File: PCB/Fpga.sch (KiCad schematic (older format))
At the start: 58 parts

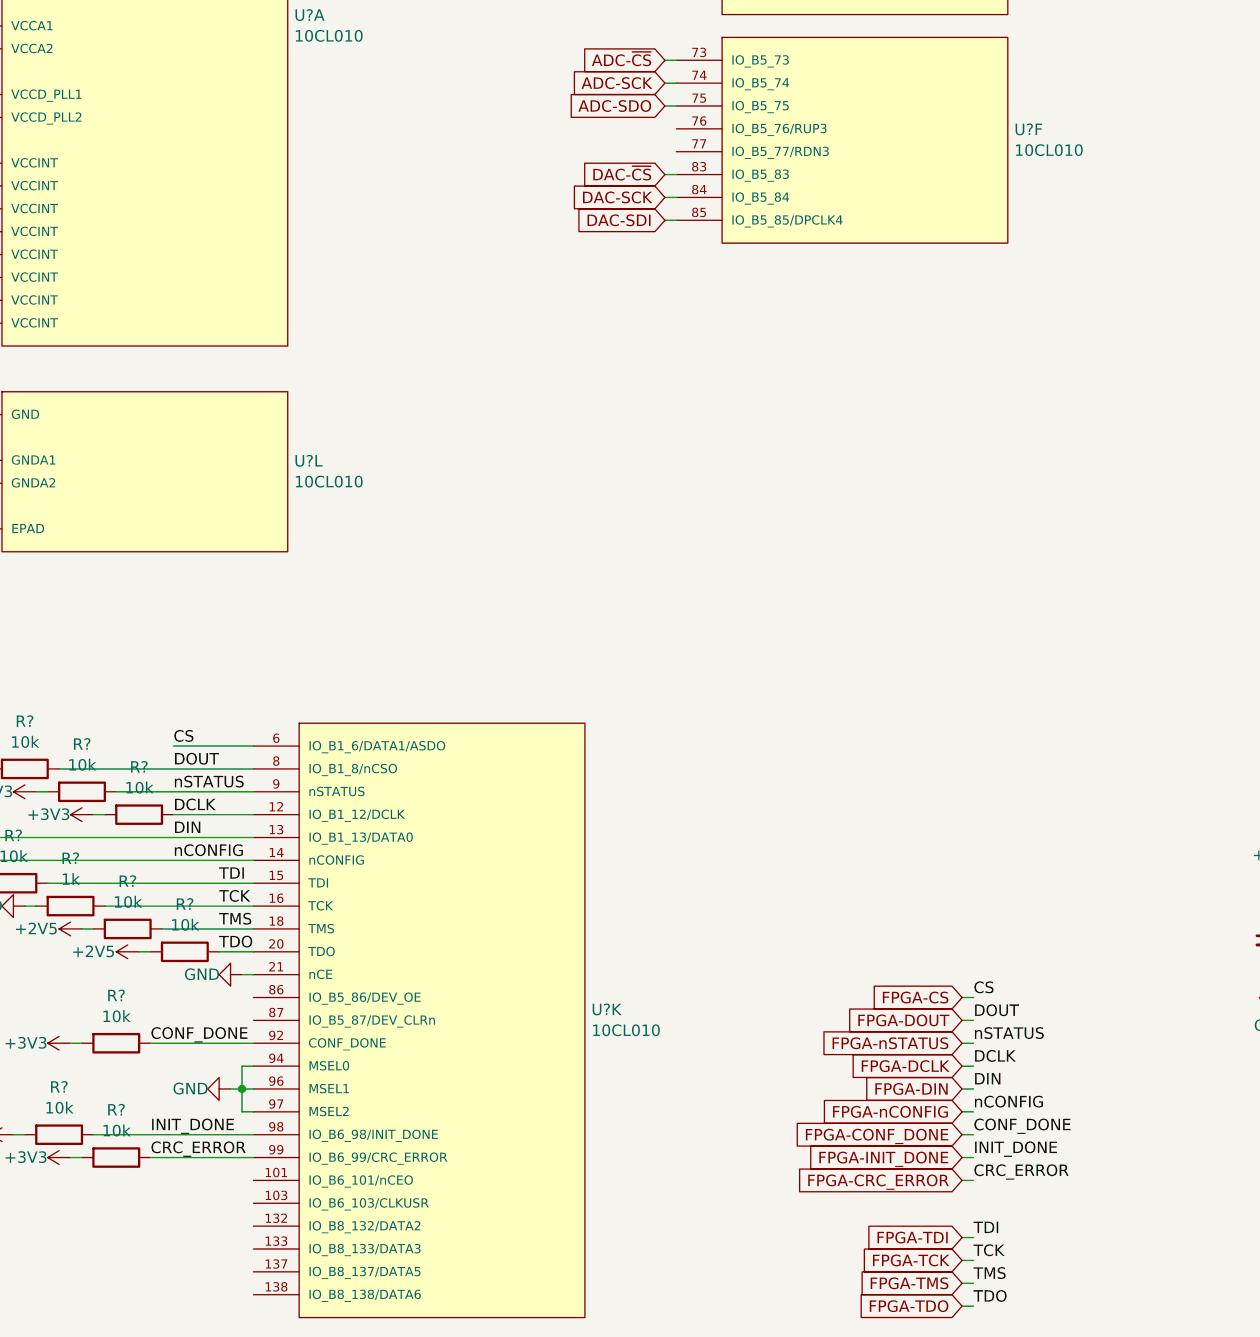
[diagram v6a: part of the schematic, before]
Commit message: Changed transmit-enable to connect to FPGA instead of microcontroller, added 10V linear regulator
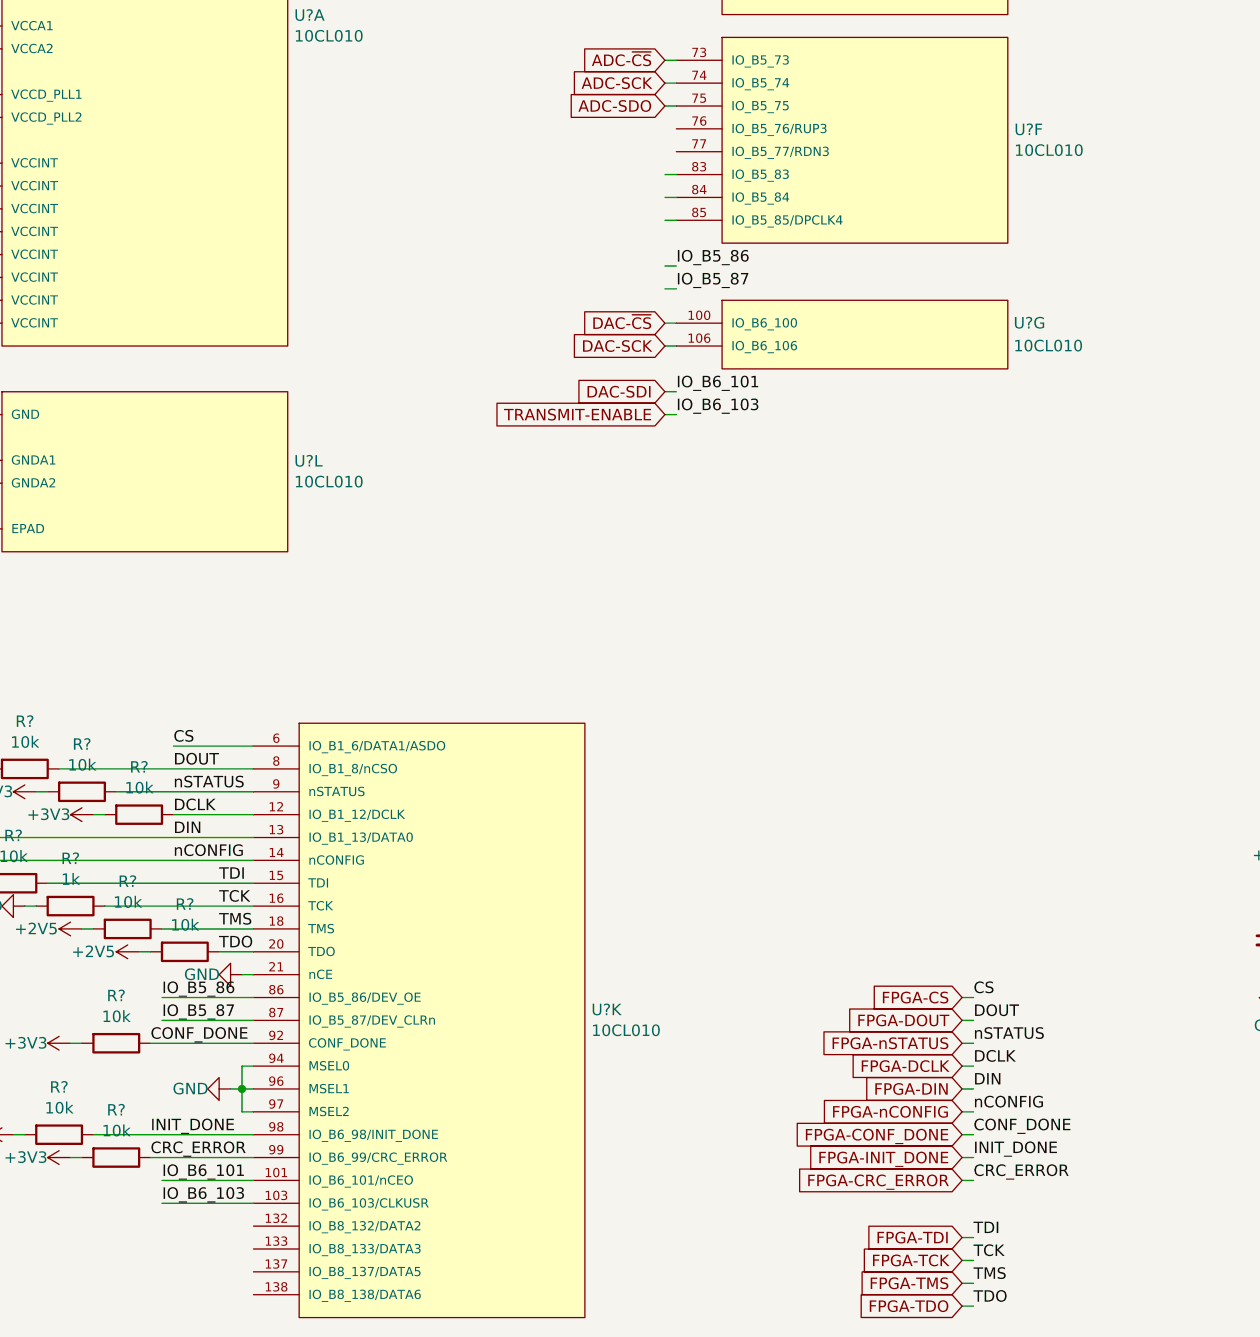
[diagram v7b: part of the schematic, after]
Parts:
- added U?: 10CL010, Parts:EQFP144-PAD, symbol Parts:10CL010
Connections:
- net DAC-SCK: now also U?.106 (IO_B6_106); no longer U?.84 (IO_B5_84)
- net DAC-SDI: now also U?.101 (IO_B6_101/nCEO); no longer U?.85 (IO_B5_85/DPCLK4)
- net DAC-~CS: now also U?.100 (IO_B6_100); no longer U?.83 (IO_B5_83)
- net TRANSMIT-ENABLE: now reaches U?.103 (IO_B6_103/CLKUSR)
- net IO_B5_86: now reaches U?.86 (IO_B5_86/DEV_OE)
- net IO_B5_87: now reaches U?.87 (IO_B5_87/DEV_CLRn)
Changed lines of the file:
@@
 Wire Wire Line
 	1300 2300 1300 2400
-Text GLabel 4450 2650 0    50   Input ~ 0
+Text GLabel 4450 3300 0    50   Input ~ 0
 DAC-~CS
-Text GLabel 4450 2750 0    50   Input ~ 0
+Text GLabel 4450 3400 0    50   Input ~ 0
 DAC-SCK
-Text GLabel 4450 2850 0    50   Input ~ 0
+Text GLabel 4450 3600 0    50   Input ~ 0
 DAC-SDI
 Text GLabel 4450 2150 0    50   Input ~ 0
@@
 Wire Wire Line
 	4450 1750 4500 1750
+Text GLabel 4450 3700 0    50   Input ~ 0
+TRANSMIT-ENABLE
+$Comp
+L Parts:10CL010 U?
+U 7 1 5DF4242E
+P 4700 3200
+F 0 "U?" H 5975 3100 50  0000 L CNN
+F 1 "10CL010" H 5975 3000 50  0000 L CNN
+F 2 "Parts:EQFP144-PAD" H 5550 3250 50  0001 L BNN
+F 3 "https://www.intel.com/content/www/us/en/programmable/products/fpga/cyclone-series/cyclone-10/cyclone-10-lp/support.html" H 4700 3200 50  0001 C CNN
+	7    4700 3200
+	1    0    0    -1
+$EndComp
+Text Label 2250 7050 0    50   ~ 0
+IO_B6_101
+Text Label 2250 7150 0    50   ~ 0
+IO_B6_103
+Wire Wire Line
+	2250 7050 2650 7050
+Wire Wire Line
+	2250 7150 2650 7150
+Text Label 4500 3600 0    50   ~ 0
+IO_B6_101
+Text Label 4500 3700 0    50   ~ 0
+IO_B6_103
+Wire Wire Line
+	4450 3300 4500 3300
+Wire Wire Line
+	4450 3400 4500 3400
+Wire Wire Line
+	4450 3600 4500 3600
+Wire Wire Line
+	4500 3700 4450 3700
+Text Label 2250 6250 0    50   ~ 0
+IO_B5_86
+Text Label 2250 6350 0    50   ~ 0
+IO_B5_87
+Wire Wire Line
+	2250 6350 2650 6350
+Wire Wire Line
+	2250 6250 2650 6250
+Text Label 4500 3050 0    50   ~ 0
+IO_B5_86
+Text Label 4500 3150 0    50   ~ 0
+IO_B5_87
+Wire Wire Line
+	4450 3050 4500 3050
+Wire Wire Line
+	4450 3150 4500 3150
 $EndSCHEMATC

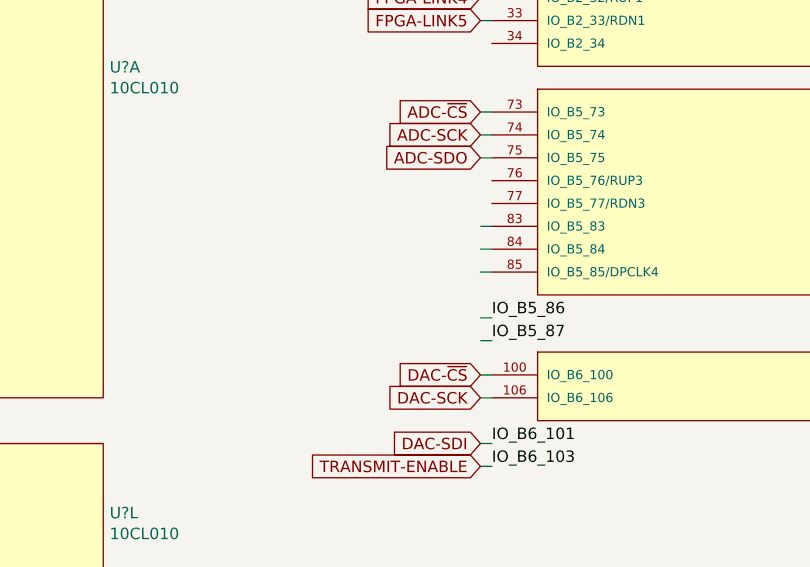
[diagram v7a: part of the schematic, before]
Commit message: Added receive amplification circuit, added opamps for receive to library, added digital potentiometer to library, connected VGA stages to FPGA
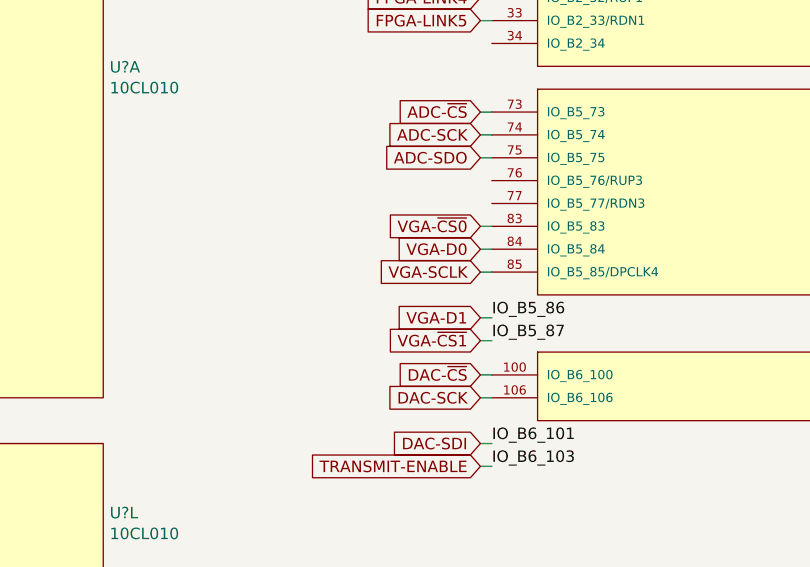
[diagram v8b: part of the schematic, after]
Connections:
- net VGA-~CS0: now reaches U?.83 (IO_B5_83)
- net VGA-D0: now reaches U?.84 (IO_B5_84)
- net VGA-SCLK: now reaches U?.85 (IO_B5_85/DPCLK4)
- net IO_B5_86 renamed VGA-D1
- net IO_B5_87 renamed VGA-~CS1
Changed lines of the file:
@@
 Wire Wire Line
 	4450 3150 4500 3150
+Text GLabel 4450 2650 0    50   Input ~ 0
+VGA-~CS0
+Text GLabel 4450 3150 0    50   Input ~ 0
+VGA-~CS1
+Text GLabel 4450 2850 0    50   Input ~ 0
+VGA-SCLK
+Text GLabel 4450 2750 0    50   Input ~ 0
+VGA-D0
+Text GLabel 4450 3050 0    50   Input ~ 0
+VGA-D1
 $EndSCHEMATC
